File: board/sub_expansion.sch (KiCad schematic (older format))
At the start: 1 part, among them J1001 Conn_02x36_Counter_Clockwise

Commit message: All footprints done
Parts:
- removed J1001: Conn_02x36_Counter_Clockwise, symbol Connector_Generic:Conn_02x36_Counter_Clockwise
- added U1001: DIN96, quokka:DIN-8609-2030, symbol quokka:DIN96
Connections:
- net labels added: +3V3, +5V
- wire segments 45 -> 91
- no-connect marks 20 -> 24

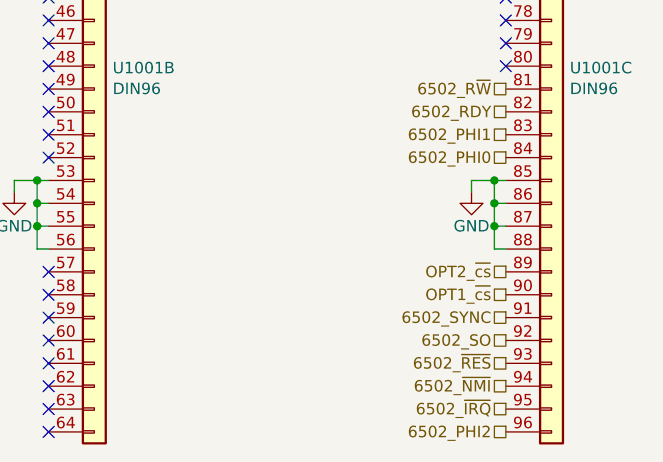
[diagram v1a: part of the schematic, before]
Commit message: Power supply routed
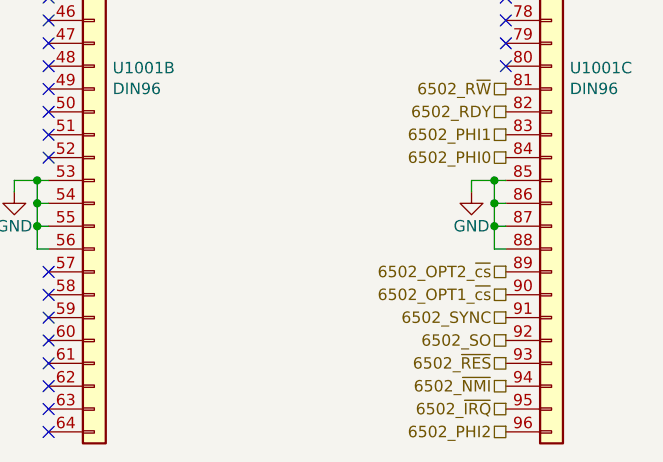
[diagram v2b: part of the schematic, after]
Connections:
- net OPT1_~cs renamed 6502_OPT1_~cs
- net OPT2_~cs renamed 6502_OPT2_~cs
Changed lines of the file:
@@
 6502_SO
 Text HLabel 8050 4800 0    50   UnSpc ~ 0
-OPT1_~cs
+6502_OPT1_~cs
 Text HLabel 8050 4700 0    50   UnSpc ~ 0
-OPT2_~cs
+6502_OPT2_~cs
 Text HLabel 8050 4900 0    50   UnSpc ~ 0
 6502_SYNC

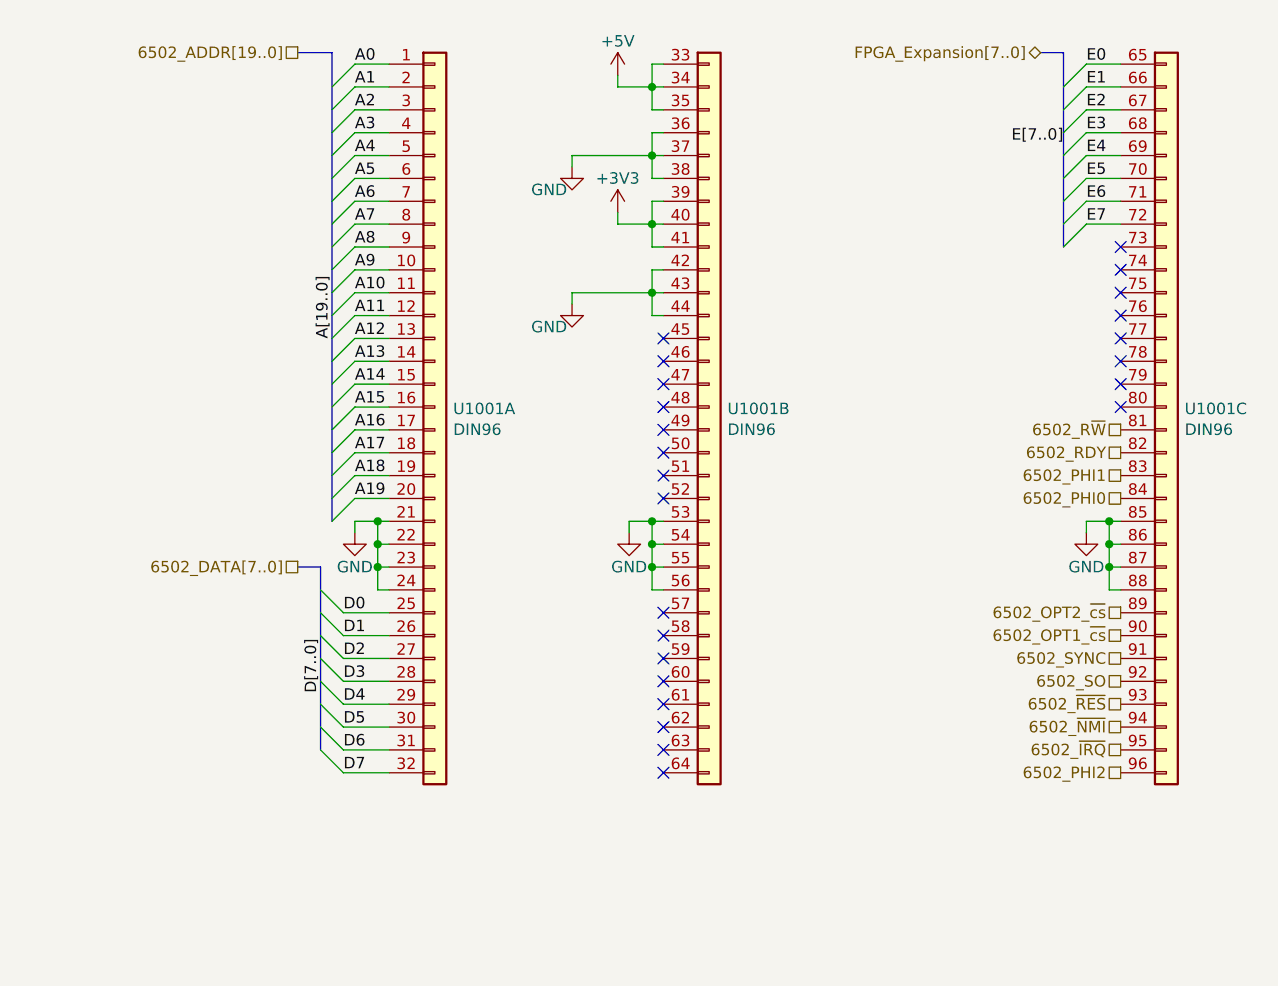
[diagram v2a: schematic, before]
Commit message: Most critical nets routed
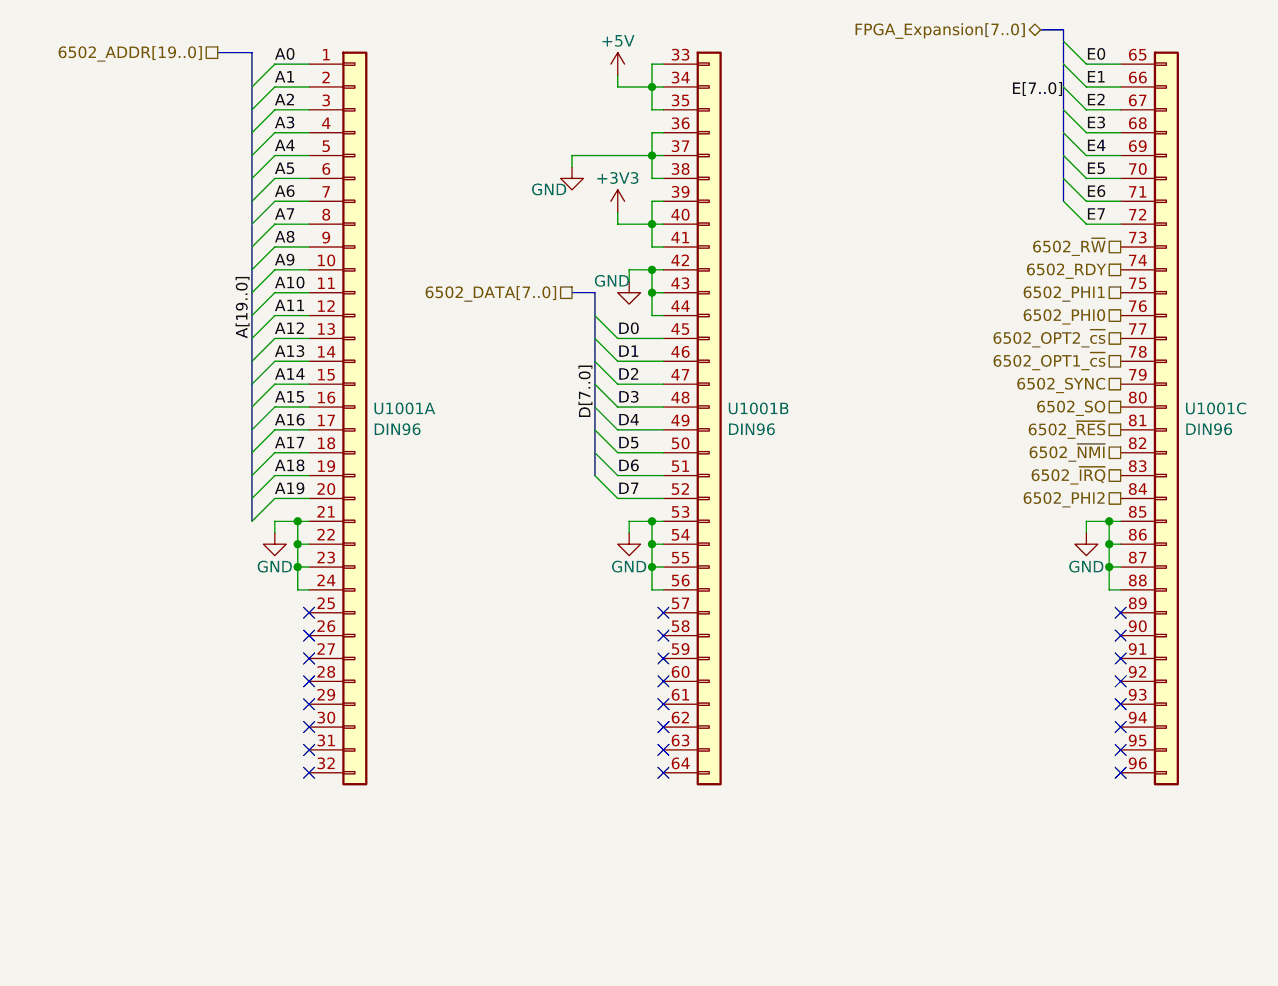
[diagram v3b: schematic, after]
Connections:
- net 6502_OPT1_~cs: now also U1001.78 (Pin_14); no longer U1001.90 (Pin_26)
- net 6502_OPT2_~cs: now also U1001.77 (Pin_13); no longer U1001.89 (Pin_25)
- net 6502_PHI0: now also U1001.76 (Pin_12); no longer U1001.84 (Pin_20)
- net 6502_PHI1: now also U1001.75 (Pin_11); no longer U1001.83 (Pin_19)
- net 6502_PHI2: now also U1001.84 (Pin_20); no longer U1001.96 (Pin_32)
- net 6502_RDY: now also U1001.74 (Pin_10); no longer U1001.82 (Pin_18)
- net 6502_R~W: now also U1001.73 (Pin_9); no longer U1001.81 (Pin_17)
- net 6502_SO: now also U1001.80 (Pin_16); no longer U1001.92 (Pin_28)
- net 6502_SYNC: now also U1001.79 (Pin_15); no longer U1001.91 (Pin_27)
- net 6502_~IRQ: now also U1001.83 (Pin_19); no longer U1001.95 (Pin_31)
- net 6502_~NMI: now also U1001.82 (Pin_18); no longer U1001.94 (Pin_30)
- net 6502_~RES: now also U1001.81 (Pin_17); no longer U1001.93 (Pin_29)
- net D0: now also U1001.45 (Pin_13); no longer U1001.25 (Pin_25)
- net D1: now also U1001.46 (Pin_14); no longer U1001.26 (Pin_26)
- net D2: now also U1001.47 (Pin_15); no longer U1001.27 (Pin_27)
- net D3: now also U1001.48 (Pin_16); no longer U1001.28 (Pin_28)
- net D4: now also U1001.49 (Pin_17); no longer U1001.29 (Pin_29)
- net D5: now also U1001.50 (Pin_18); no longer U1001.30 (Pin_30)
- net D6: now also U1001.51 (Pin_19); no longer U1001.31 (Pin_31)
- net D7: now also U1001.52 (Pin_20); no longer U1001.32 (Pin_32)
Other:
- moved on the sheet: U1001A

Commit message: Cleaned up silkscreen designators
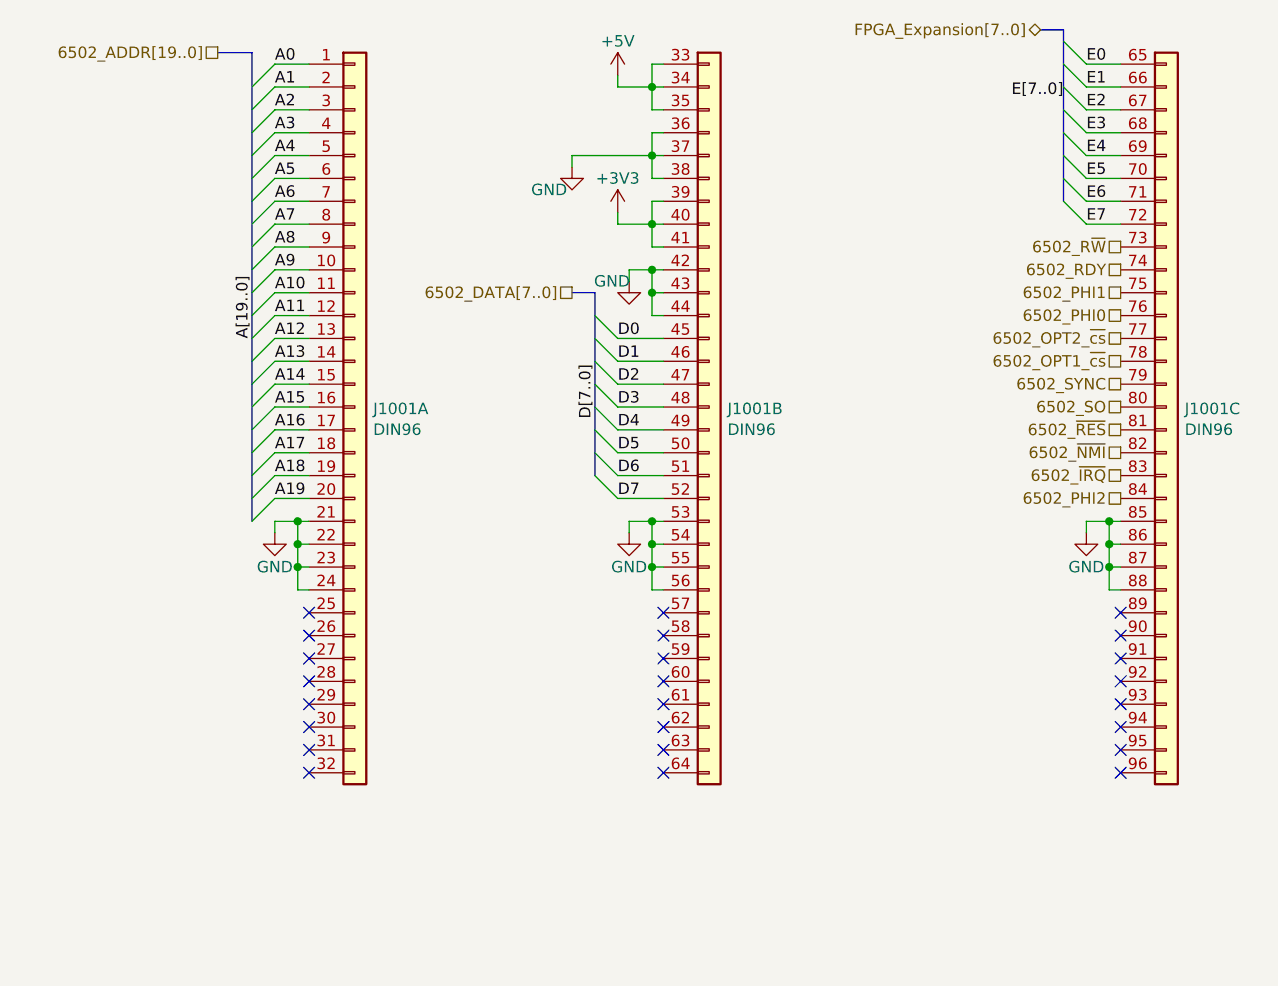
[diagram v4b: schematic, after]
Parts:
- renumbered U1001 to J1001
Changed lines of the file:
@@
 Connection ~ 4450 4400
 $Comp
-L quokka:DIN96 U1001
+L quokka:DIN96 J1001
 U 1 1 5AAF3BC6
 P 4700 3800
-F 0 "U1001" H 4780 3792 50  0000 L CNN
+F 0 "J1001" H 4780 3792 50  0000 L CNN
 F 1 "DIN96" H 4780 3701 50  0000 L CNN
 F 2 "quokka:DIN-8609-2030" H 4850 4200 50  0001 C CNN
@@
 $EndComp
 $Comp
-L quokka:DIN96 U1001
+L quokka:DIN96 J1001
 U 3 1 5AAF3D79
 P 8250 3800
-F 0 "U1001" H 8330 3792 50  0000 L CNN
+F 0 "J1001" H 8330 3792 50  0000 L CNN
 F 1 "DIN96" H 8330 3701 50  0000 L CNN
 F 2 "quokka:DIN-8609-2030" H 8400 4200 50  0001 C CNN
@@
 NoConn ~ 6050 5400
 $Comp
-L quokka:DIN96 U1001
+L quokka:DIN96 J1001
 U 2 1 5AAF3CCF
 P 6250 3800
-F 0 "U1001" H 6330 3792 50  0000 L CNN
+F 0 "J1001" H 6330 3792 50  0000 L CNN
 F 1 "DIN96" H 6330 3701 50  0000 L CNN
 F 2 "quokka:DIN-8609-2030" H 6400 4200 50  0001 C CNN
